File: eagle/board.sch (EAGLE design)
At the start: 6 parts, among them J1 M20X2SHROUDED

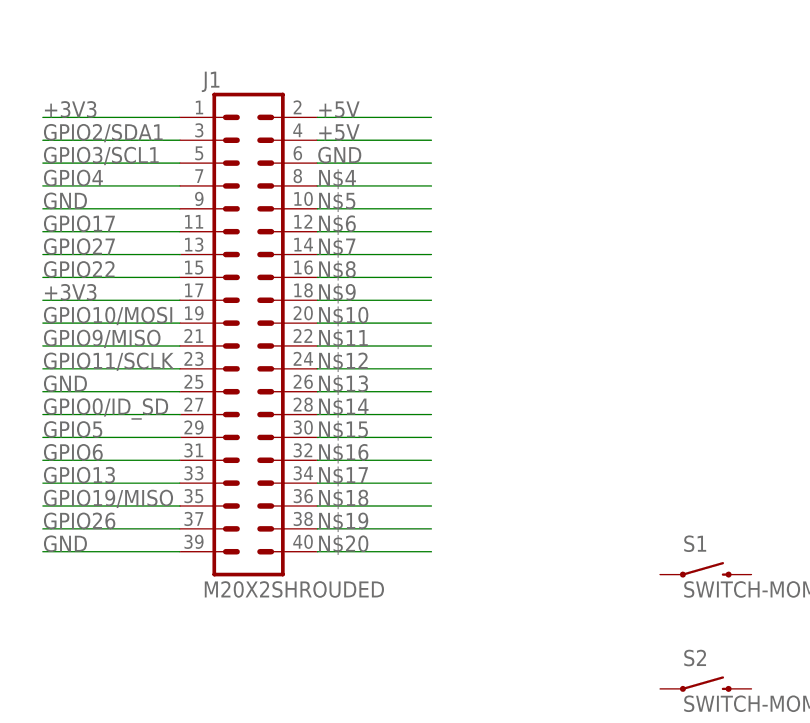
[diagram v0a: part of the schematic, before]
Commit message: Adding rest of IO labels to board
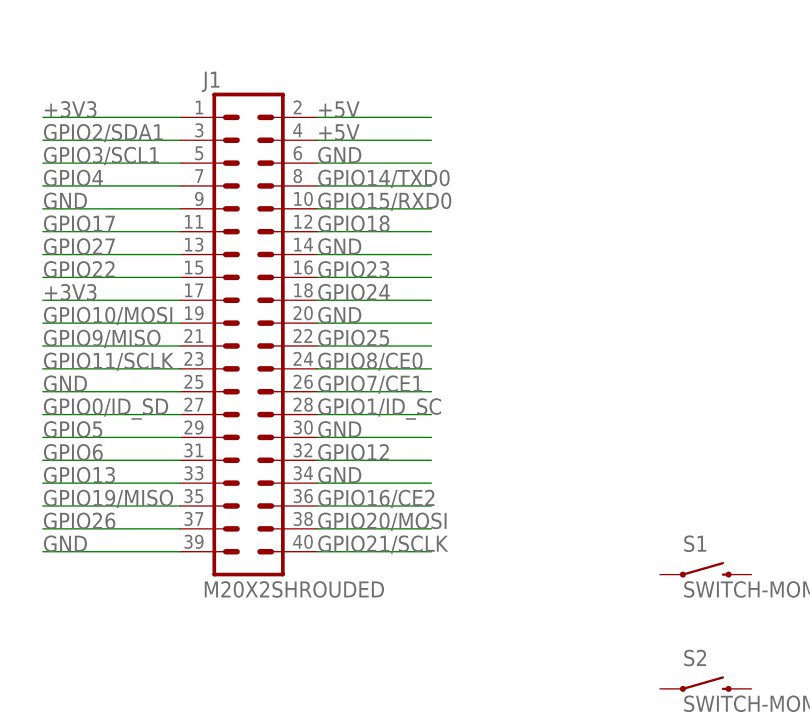
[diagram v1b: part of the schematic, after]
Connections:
- net N$11 renamed GPIO25
- net N$12 renamed GPIO8/CE0
- net N$13 renamed GPIO7/CE1
- net N$14 renamed GPIO1/ID_SC
- net N$16 renamed GPIO12
- net N$18 renamed GPIO16/CE2
- net N$19 renamed GPIO20/MOSI
- net N$20 renamed GPIO21/SCLK
- net N$4 renamed GPIO14/TXD0
- net N$5 renamed GPIO15/RXD0
- net N$6 renamed GPIO18
- net N$8 renamed GPIO23
- net N$9 renamed GPIO24
- removed net N$10: J1.20
- removed net N$15: J1.30
- removed net N$17: J1.34
- removed net N$7: J1.14
- net GND: now also J1.14, J1.20, J1.30, J1.34
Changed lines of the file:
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@@
 <grid distance="0.1" unitdist="inch" unit="inch" style="lines" multiple="1" display="no" altdistance="0.01" altunitdist="inch" altunit="inch"/>
 <layers>
-<layer number="1" name="Top" color="4" fill="1" visible="yes" active="no"/>
-<layer number="16" name="Bottom" color="1" fill="1" visible="yes" active="no"/>
-<layer number="17" name="Pads" color="2" fill="1" visible="yes" active="no"/>
-<layer number="18" name="Vias" color="2" fill="1" visible="yes" active="no"/>
-<layer number="19" name="Unrouted" color="6" fill="1" visible="yes" active="no"/>
-<layer number="20" name="Dimension" color="15" fill="1" visible="yes" active="no"/>
-<layer number="21" name="tPlace" color="7" fill="1" visible="yes" active="no"/>
-<layer number="22" name="bPlace" color="7" fill="1" visible="yes" active="no"/>
-<layer number="23" name="tOrigins" color="15" fill="1" visible="yes" active="no"/>
-<layer number="24" name="bOrigins" color="15" fill="1" visible="yes" active="no"/>
-<layer number="25" name="tNames" color="7" fill="1" visible="yes" active="no"/>
-<layer number="26" name="bNames" color="7" fill="1" visible="yes" active="no"/>
-<layer number="27" name="tValues" color="7" fill="1" visible="yes" active="no"/>
-<layer number="28" name="bValues" color="7" fill="1" visible="yes" active="no"/>
+<layer number="1" name="Top" color="4" fill="1" visible="no" active="no"/>
+<layer number="16" name="Bottom" color="1" fill="1" visible="no" active="no"/>
+<layer number="17" name="Pads" color="2" fill="1" visible="no" active="no"/>
+<layer number="18" name="Vias" color="2" fill="1" visible="no" active="no"/>
+<layer number="19" name="Unrouted" color="6" fill="1" visible="no" active="no"/>
+<layer number="20" name="Dimension" color="15" fill="1" visible="no" active="no"/>
+<layer number="21" name="tPlace" color="7" fill="1" visible="no" active="no"/>
+<layer number="22" name="bPlace" color="7" fill="1" visible="no" active="no"/>
+<layer number="23" name="tOrigins" color="15" fill="1" visible="no" active="no"/>
+<layer number="24" name="bOrigins" color="15" fill="1" visible="no" active="no"/>
+<layer number="25" name="tNames" color="7" fill="1" visible="no" active="no"/>
+<layer number="26" name="bNames" color="7" fill="1" visible="no" active="no"/>
+<layer number="27" name="tValues" color="7" fill="1" visible="no" active="no"/>
+<layer number="28" name="bValues" color="7" fill="1" visible="no" active="no"/>
 <layer number="29" name="tStop" color="7" fill="3" visible="no" active="no"/>
 <layer number="30" name="bStop" color="7" fill="6" visible="no" active="no"/>
@@
 <layer number="35" name="tGlue" color="7" fill="4" visible="no" active="no"/>
 <layer number="36" name="bGlue" color="7" fill="5" visible="no" active="no"/>
-<layer number="37" name="tTest" color="7" fill="1" visible="yes" active="no"/>
-<layer number="38" name="bTest" color="7" fill="1" visible="yes" active="no"/>
+<layer number="37" name="tTest" color="7" fill="1" visible="no" active="no"/>
+<layer number="38" name="bTest" color="7" fill="1" visible="no" active="no"/>
 <layer number="39" name="tKeepout" color="4" fill="11" visible="no" active="no"/>
 <layer number="40" name="bKeepout" color="1" fill="11" visible="no" active="no"/>
@@
 <layer number="44" name="Drills" color="7" fill="1" visible="no" active="no"/>
 <layer number="45" name="Holes" color="7" fill="1" visible="no" active="no"/>
-<layer number="46" name="Milling" color="3" fill="1" visible="yes" active="no"/>
-<layer number="47" name="Measures" color="7" fill="1" visible="yes" active="no"/>
-<layer number="48" name="Document" color="7" fill="1" visible="yes" active="no"/>
-<layer number="49" name="Reference" color="7" fill="1" visible="yes" active="no"/>
-<layer number="50" name="dxf" color="7" fill="1" visible="yes" active="no"/>
-<layer number="51" name="tDocu" color="7" fill="1" visible="yes" active="no"/>
-<layer number="52" name="bDocu" color="7" fill="1" visible="yes" active="no"/>
-<layer number="53" name="tGND_GNDA" color="7" fill="9" visible="yes" active="no"/>
-<layer number="54" name="bGND_GNDA" color="1" fill="9" visible="yes" active="no"/>
-<layer number="56" name="wert" color="7" fill="1" visible="yes" active="no"/>
-<layer number="57" name="tCAD" color="7" fill="1" visible="yes" active="no"/>
-<layer number="59" name="tCarbon" color="7" fill="1" visible="yes" active="no"/>
-<layer number="60" name="bCarbon" color="7" fill="1" visible="yes" active="no"/>
+<layer number="46" name="Milling" color="3" fill="1" visible="no" active="no"/>
+<layer number="47" name="Measures" color="7" fill="1" visible="no" active="no"/>
+<layer number="48" name="Document" color="7" fill="1" visible="no" active="no"/>
+<layer number="49" name="Reference" color="7" fill="1" visible="no" active="no"/>
+<layer number="50" name="dxf" color="7" fill="1" visible="no" active="no"/>
+<layer number="51" name="tDocu" color="7" fill="1" visible="no" active="no"/>
+<layer number="52" name="bDocu" color="7" fill="1" visible="no" active="no"/>
+<layer number="53" name="tGND_GNDA" color="7" fill="9" visible="no" active="no"/>
+<layer number="54" name="bGND_GNDA" color="1" fill="9" visible="no" active="no"/>
+<layer number="56" name="wert" color="7" fill="1" visible="no" active="no"/>
+<layer number="57" name="tCAD" color="7" fill="1" visible="no" active="no"/>
+<layer number="59" name="tCarbon" color="7" fill="1" visible="no" active="no"/>
+<layer number="60" name="bCarbon" color="7" fill="1" visible="no" active="no"/>
 <layer number="90" name="Modules" color="5" fill="1" visible="yes" active="yes"/>
 <layer number="91" name="Nets" color="2" fill="1" visible="yes" active="yes"/>
@@
 <label x="45.72" y="83.82" size="1.778" layer="95"/>
 </segment>
-</net>
-<net name="N$4" class="0">
+<segment>
+<pinref part="J1" gate="G$1" pin="14"/>
+<wire x1="76.2" y1="99.06" x2="88.9" y2="99.06" width="0.1524" layer="91"/>
+<label x="76.2" y="99.06" size="1.778" layer="95"/>
+</segment>
+<segment>
+<pinref part="J1" gate="G$1" pin="20"/>
+<wire x1="76.2" y1="91.44" x2="88.9" y2="91.44" width="0.1524" layer="91"/>
+<label x="76.2" y="91.44" size="1.778" layer="95"/>
+</segment>
+<segment>
+<pinref part="J1" gate="G$1" pin="30"/>
+<wire x1="76.2" y1="78.74" x2="88.9" y2="78.74" width="0.1524" layer="91"/>
+<label x="76.2" y="78.74" size="1.778" layer="95"/>
+</segment>
+<segment>
+<pinref part="J1" gate="G$1" pin="34"/>
+<wire x1="76.2" y1="73.66" x2="88.9" y2="73.66" width="0.1524" layer="91"/>
+<label x="76.2" y="73.66" size="1.778" layer="95"/>
+</segment>
+</net>
+<net name="GPIO14/TXD0" class="0">
 <segment>
 <pinref part="J1" gate="G$1" pin="8"/>
@@
 </segment>
 </net>
-<net name="N$5" class="0">
+<net name="GPIO15/RXD0" class="0">
 <segment>
 <pinref part="J1" gate="G$1" pin="10"/>
@@
 </segment>
 </net>
-<net name="N$6" class="0">
+<net name="GPIO18" class="0">
 <segment>
 <pinref part="J1" gate="G$1" pin="12"/>
@@
 </segment>
 </net>
-<net name="N$7" class="0">
-<segment>
-<pinref part="J1" gate="G$1" pin="14"/>
-<wire x1="76.2" y1="99.06" x2="88.9" y2="99.06" width="0.1524" layer="91"/>
-<label x="76.2" y="99.06" size="1.778" layer="95"/>
-</segment>
-</net>
-<net name="N$8" class="0">
+<net name="GPIO23" class="0">
 <segment>
 <pinref part="J1" gate="G$1" pin="16"/>
@@
 </segment>
 </net>
-<net name="N$9" class="0">
+<net name="GPIO24" class="0">
 <segment>
 <pinref part="J1" gate="G$1" pin="18"/>
@@
 </segment>
 </net>
-<net name="N$10" class="0">
-<segment>
-<pinref part="J1" gate="G$1" pin="20"/>
-<wire x1="76.2" y1="91.44" x2="88.9" y2="91.44" width="0.1524" layer="91"/>
-<label x="76.2" y="91.44" size="1.778" layer="95"/>
-</segment>
-</net>
-<net name="N$11" class="0">
+<net name="GPIO25" class="0">
 <segment>
 <pinref part="J1" gate="G$1" pin="22"/>
@@
 </segment>
 </net>
-<net name="N$12" class="0">
+<net name="GPIO8/CE0" class="0">
 <segment>
 <pinref part="J1" gate="G$1" pin="24"/>
@@
 </segment>
 </net>
-<net name="N$13" class="0">
+<net name="GPIO7/CE1" class="0">
 <segment>
 <pinref part="J1" gate="G$1" pin="26"/>
@@
 </segment>
 </net>
-<net name="N$14" class="0">
+<net name="GPIO1/ID_SC" class="0">
 <segment>
 <pinref part="J1" gate="G$1" pin="28"/>
@@
 </segment>
 </net>
-<net name="N$15" class="0">
-<segment>
-<pinref part="J1" gate="G$1" pin="30"/>
-<wire x1="76.2" y1="78.74" x2="88.9" y2="78.74" width="0.1524" layer="91"/>
-<label x="76.2" y="78.74" size="1.778" layer="95"/>
-</segment>
-</net>
-<net name="N$16" class="0">
+<net name="GPIO12" class="0">
 <segment>
 <pinref part="J1" gate="G$1" pin="32"/>
@@
 </segment>
 </net>
-<net name="N$17" class="0">
-<segment>
-<pinref part="J1" gate="G$1" pin="34"/>
-<wire x1="76.2" y1="73.66" x2="88.9" y2="73.66" width="0.1524" layer="91"/>
-<label x="76.2" y="73.66" size="1.778" layer="95"/>
-</segment>
-</net>
-<net name="N$18" class="0">
+<net name="GPIO16/CE2" class="0">
 <segment>
 <pinref part="J1" gate="G$1" pin="36"/>
@@
 </segment>
 </net>
-<net name="N$19" class="0">
+<net name="GPIO20/MOSI" class="0">
 <segment>
 <pinref part="J1" gate="G$1" pin="38"/>
@@
 </segment>
 </net>
-<net name="N$20" class="0">
+<net name="GPIO21/SCLK" class="0">
 <segment>
 <pinref part="J1" gate="G$1" pin="40"/>

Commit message: Renaming gnd/pwr signals so they don't route together
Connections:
- removed net +3V3: J1.1, J1.17
- removed net +5V: J1.2, J1.4
- removed net GND: J1.14, J1.20, J1.25, J1.30, J1.34, J1.39, J1.6, J1.9
- new net +3V3_0: J1.1
- new net +3V3_1: J1.17
- new net +5V_0: J1.2
- new net +5V_1: J1.4
- new net GND0: J1.9
- new net GND1: J1.25
- new net GND2: J1.39
- new net GND3: J1.6
- new net GND4: J1.14
- new net GND5: J1.20
- new net GND6: J1.30
- new net GND7: J1.34

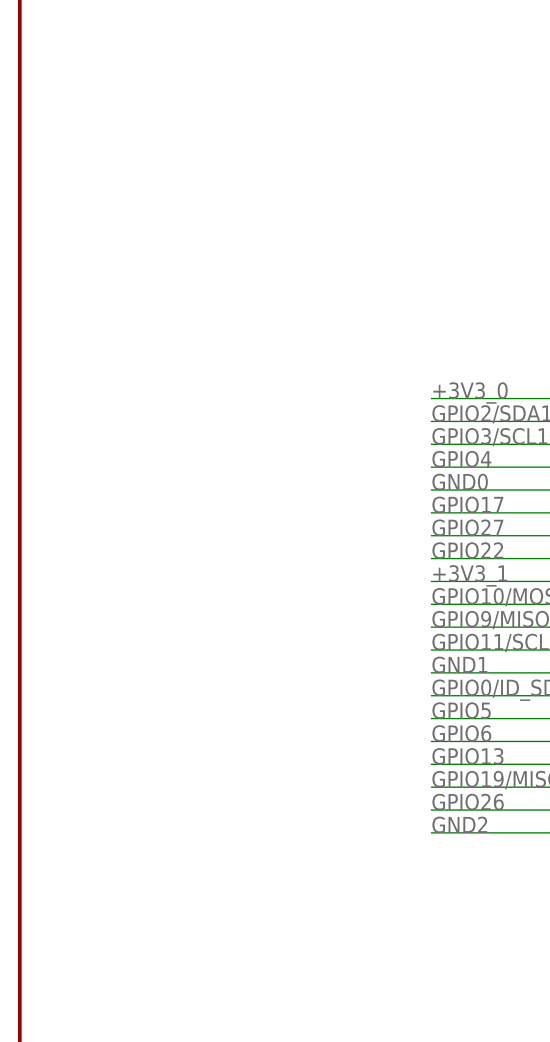
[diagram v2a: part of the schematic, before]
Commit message: Adding headers for modules
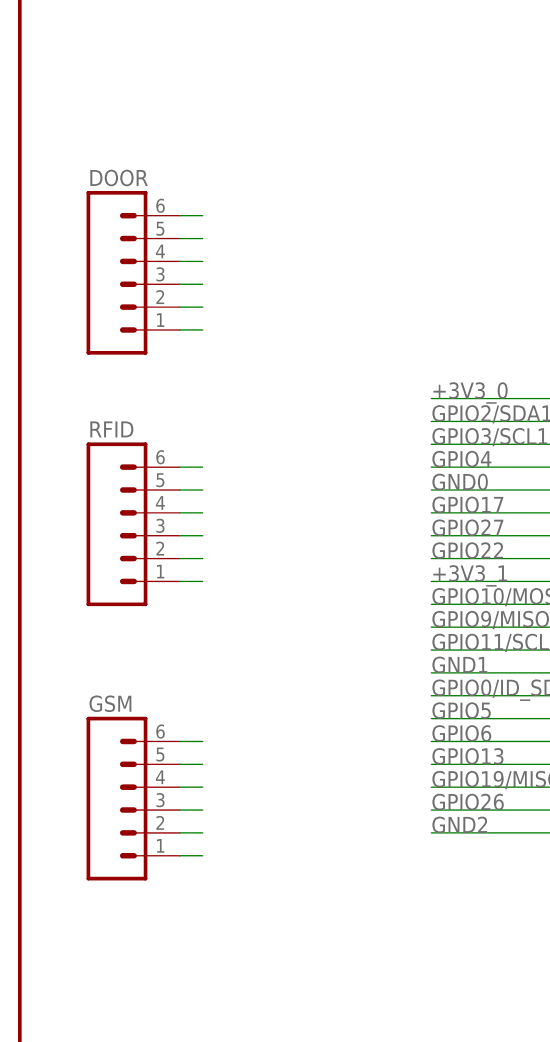
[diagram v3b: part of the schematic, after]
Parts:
- added DOOR, GSM, RFID: (no value), SparkFun-Connectors:M06LOCK
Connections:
- new net N$1: DOOR.6
- new net N$10: RFID.3
- new net N$11: RFID.2
- new net N$12: RFID.1
- new net N$13: GSM.6
- new net N$14: GSM.5
- new net N$15: GSM.4
- new net N$16: GSM.3
- new net N$17: GSM.2
- new net N$18: GSM.1
- new net N$2: DOOR.5
- new net N$3: DOOR.4
- new net N$4: DOOR.3
- new net N$5: DOOR.2
- new net N$6: DOOR.1
- new net N$7: RFID.6
- new net N$8: RFID.5
- new net N$9: RFID.4
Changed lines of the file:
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@@
 <part name="D1" library="SparkFun-LED" deviceset="LED" device="5MM"/>
 <part name="D2" library="SparkFun-LED" deviceset="LED" device="5MM"/>
+<part name="DOOR" library="SparkFun-Connectors" deviceset="M06" device="LOCK"/>
+<part name="RFID" library="SparkFun-Connectors" deviceset="M06" device="LOCK"/>
+<part name="GSM" library="SparkFun-Connectors" deviceset="M06" device="LOCK"/>
 </parts>
 <sheets>
@@
 <instance part="D1" gate="G$1" x="109.22" y="134.62"/>
 <instance part="D2" gate="G$1" x="124.46" y="134.62"/>
+<instance part="DOOR" gate="G$1" x="12.7" y="127"/>
+<instance part="RFID" gate="G$1" x="12.7" y="99.06"/>
+<instance part="GSM" gate="G$1" x="12.7" y="68.58"/>
 </instances>
 <busses>
@@
 </segment>
 </net>
+<net name="N$1" class="0">
+<segment>
+<pinref part="DOOR" gate="G$1" pin="6"/>
+<wire x1="17.78" y1="134.62" x2="20.32" y2="134.62" width="0.1524" layer="91"/>
+</segment>
+</net>
+<net name="N$2" class="0">
+<segment>
+<pinref part="DOOR" gate="G$1" pin="5"/>
+<wire x1="17.78" y1="132.08" x2="20.32" y2="132.08" width="0.1524" layer="91"/>
+</segment>
+</net>
+<net name="N$3" class="0">
+<segment>
+<pinref part="DOOR" gate="G$1" pin="4"/>
+<wire x1="17.78" y1="129.54" x2="20.32" y2="129.54" width="0.1524" layer="91"/>
+</segment>
+</net>
+<net name="N$4" class="0">
+<segment>
+<pinref part="DOOR" gate="G$1" pin="3"/>
+<wire x1="17.78" y1="127" x2="20.32" y2="127" width="0.1524" layer="91"/>
+</segment>
+</net>
+<net name="N$5" class="0">
+<segment>
+<pinref part="DOOR" gate="G$1" pin="2"/>
+<wire x1="17.78" y1="124.46" x2="20.32" y2="124.46" width="0.1524" layer="91"/>
+</segment>
+</net>
+<net name="N$6" class="0">
+<segment>
+<pinref part="DOOR" gate="G$1" pin="1"/>
+<wire x1="17.78" y1="121.92" x2="20.32" y2="121.92" width="0.1524" layer="91"/>
+</segment>
+</net>
+<net name="N$7" class="0">
+<segment>
+<pinref part="RFID" gate="G$1" pin="6"/>
+<wire x1="17.78" y1="106.68" x2="20.32" y2="106.68" width="0.1524" layer="91"/>
+</segment>
+</net>
+<net name="N$8" class="0">
+<segment>
+<pinref part="RFID" gate="G$1" pin="5"/>
+<wire x1="17.78" y1="104.14" x2="20.32" y2="104.14" width="0.1524" layer="91"/>
+</segment>
+</net>
+<net name="N$9" class="0">
+<segment>
+<pinref part="RFID" gate="G$1" pin="4"/>
+<wire x1="17.78" y1="101.6" x2="20.32" y2="101.6" width="0.1524" layer="91"/>
+</segment>
+</net>
+<net name="N$10" class="0">
+<segment>
+<pinref part="RFID" gate="G$1" pin="3"/>
+<wire x1="17.78" y1="99.06" x2="20.32" y2="99.06" width="0.1524" layer="91"/>
+</segment>
+</net>
+<net name="N$11" class="0">
+<segment>
+<pinref part="RFID" gate="G$1" pin="2"/>
+<wire x1="17.78" y1="96.52" x2="20.32" y2="96.52" width="0.1524" layer="91"/>
+</segment>
+</net>
+<net name="N$12" class="0">
+<segment>
+<pinref part="RFID" gate="G$1" pin="1"/>
+<wire x1="17.78" y1="93.98" x2="20.32" y2="93.98" width="0.1524" layer="91"/>
+</segment>
+</net>
+<net name="N$13" class="0">
+<segment>
+<pinref part="GSM" gate="G$1" pin="6"/>
+<wire x1="17.78" y1="76.2" x2="20.32" y2="76.2" width="0.1524" layer="91"/>
+</segment>
+</net>
+<net name="N$14" class="0">
+<segment>
+<pinref part="GSM" gate="G$1" pin="5"/>
+<wire x1="17.78" y1="73.66" x2="20.32" y2="73.66" width="0.1524" layer="91"/>
+</segment>
+</net>
+<net name="N$15" class="0">
+<segment>
+<pinref part="GSM" gate="G$1" pin="4"/>
+<wire x1="17.78" y1="71.12" x2="20.32" y2="71.12" width="0.1524" layer="91"/>
+</segment>
+</net>
+<net name="N$16" class="0">
+<segment>
+<pinref part="GSM" gate="G$1" pin="3"/>
+<wire x1="20.32" y1="68.58" x2="17.78" y2="68.58" width="0.1524" layer="91"/>
+</segment>
+</net>
+<net name="N$17" class="0">
+<segment>
+<pinref part="GSM" gate="G$1" pin="2"/>
+<wire x1="17.78" y1="66.04" x2="20.32" y2="66.04" width="0.1524" layer="91"/>
+</segment>
+</net>
+<net name="N$18" class="0">
+<segment>
+<pinref part="GSM" gate="G$1" pin="1"/>
+<wire x1="17.78" y1="63.5" x2="20.32" y2="63.5" width="0.1524" layer="91"/>
+</segment>
+</net>
